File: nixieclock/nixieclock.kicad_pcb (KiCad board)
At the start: 4 copper layers, 91 parts, among them Q1 AO3401A, Q10 BSS131, Q11 BSS131, Q12 BSS131, Q13 BSS131, Q14 BSS131, Q15 BSS131, Q16 BSS131, Q17 BSS131, Q18 BSS131, Q19 BSS131, Q2 IRLR3110ZTRPBF, Q20 BSS131, Q21 BSS131, Q22 BSS131, Q23 BSS131, Q24 BSS131, Q25 BSS131, Q26 BSS131, Q27 BSS131, Q28 BSS131, Q29 BSS131, Q3 BSS131, Q30 BSS131, Q31 BSS131, Q32 BSS131, Q33 BSS131, Q34 BSS131, Q35 BSS131, Q36 BSS131, Q37 BSS131, Q38 BSS131, Q39 BSS131, Q4 BSS131, Q40 BSS131, Q41 BSS131, Q42 BSS131, Q5 BSS131, Q6 BSS131, Q7 BSS131, Q8 BSS131, Q9 BSS131, U1 LT3757AEMSE, U2 AMS1117-3.3, U3 74HC595, U4 74HC595, U5 74HC595, U6 74HC595, U7 74HC595, U8 STM32F058R8Tx

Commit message: mostly finalized pcb layout, silkscreen graphics, etc
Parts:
- added BT1: Battery_Cell, Battery:BatteryHolder_Keystone_3000_1x12mm, F.Cu at (130.0, 99.0)
- added C20: 100nF, Capacitor_SMD:C_0603_1608Metric_Pad1.05x0.95mm_HandSolder, F.Cu at (139.4, 103.4)
- added C21: 100nF, Capacitor_SMD:C_0603_1608Metric_Pad1.05x0.95mm_HandSolder, F.Cu at (154.6, 94.6)
- added C22: 10nF, Capacitor_SMD:C_0603_1608Metric_Pad1.05x0.95mm_HandSolder, F.Cu at (149.0, 106.6)
- added C23: 1uF, Capacitor_SMD:C_0603_1608Metric_Pad1.05x0.95mm_HandSolder, F.Cu at (149.0, 108.2)
- added C24: 100nF, Capacitor_SMD:C_0603_1608Metric_Pad1.05x0.95mm_HandSolder, F.Cu at (146.2, 107.4)
- added G**: ARM-JTAG-10-SILK, Personal:ARM-JTAG-10-SILK, F.Cu at (152.6, 84.8)
- added G***: LOGO, nixieclock_graphics:high_voltage, F.Cu at (117.1, 93.4)
- added G***: LOGO, nixieclock_graphics:db_logo, F.Cu at (122.0, 80.0)
- added J1: USB_C_Receptacle, Connector_USB:USB_C_Receptacle_Amphenol_12401610E4-2A, F.Cu at (80.4, 75.0)
- added J2: Conn_ARM_JTAG_SWD_10, Connector_PinHeader_2.54mm:PinHeader_2x05_P2.54mm_Vertical_SMD, F.Cu at (139.2, 84.8)
- added R14: 10k, Resistor_SMD:R_0603_1608Metric_Pad1.05x0.95mm_HandSolder, F.Cu at (139.4, 100.0)
- U8: value STM32F058R8Tx -> STM32F051R4Tx
- moved C14 62.4 mm to (105.0, 75.3), turned to 180 degrees
- moved F1 61.6 mm to (88.1, 79.9), turned to 0 degrees
- moved Q1 58.4 mm to (93.0, 79.9), turned to 180 degrees
- moved FB1 56.4 mm to (96.5, 80.0), turned to 90 degrees
- moved C13 56.3 mm to (99.0, 80.0), turned to 90 degrees
- moved U2 55.7 mm to (105.0, 80.0), turned to 0 degrees
- moved C5 52.1 mm to (95.0, 83.9), turned to 180 degrees
- moved C18 39.0 mm to (134.4, 159.7), turned to 90 degrees
- moved C16 38.9 mm to (101.0, 159.7), turned to 90 degrees
- moved C17 37.3 mm to (116.0, 152.0), turned to 90 degrees
- moved C15 37.1 mm to (83.5, 162.5), turned to 0 degrees
- moved C19 37.0 mm to (150.0, 162.5), turned to 0 degrees
- moved Q2 36.1 mm to (71.0, 101.1)
- moved C1 36.1 mm to (79.5, 87.0)
- moved C10 36.1 mm to (69.2, 86.4)
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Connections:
- F1 pad 1: (no net) -> +5V
- R3 pad 1: VCC -> +3V3
- R3 pad 2: ~SHDN -> /microcontroller/~SHDN
- U1 pad 9: ~SHDN -> /microcontroller/~SHDN
- U3 pad 14: (no net) -> /cathode_registers/D
- U8 pad 1: unconnected-(U8-Pad1) -> /microcontroller/VBAT
- U8 pad 10: unconnected-(U8-Pad10) -> (no net)
- U8 pad 11: unconnected-(U8-Pad11) -> (no net)
- U8 pad 12: unconnected-(U8-Pad12) -> GND
- U8 pad 13: unconnected-(U8-Pad13) -> +3V3
- U8 pad 14: unconnected-(U8-Pad14) -> /cathode_registers/~OE
- U8 pad 15: unconnected-(U8-Pad15) -> /cathode_registers/~RES
- U8 pad 16: unconnected-(U8-Pad16) -> /cathode_registers/LCLK
- U8 pad 17: unconnected-(U8-Pad17) -> /microcontroller/~SHDN
- U8 pad 18: unconnected-(U8-Pad18) -> (no net)
- U8 pad 19: unconnected-(U8-Pad19) -> (no net)
- U8 pad 2: unconnected-(U8-Pad2) -> (no net)
- U8 pad 20: unconnected-(U8-Pad20) -> (no net)
- U8 pad 21: unconnected-(U8-Pad21) -> /cathode_registers/CLK
- U8 pad 22: unconnected-(U8-Pad22) -> (no net)
- U8 pad 23: unconnected-(U8-Pad23) -> /cathode_registers/D
- U8 pad 24: unconnected-(U8-Pad24) -> (no net)
- U8 pad 25: unconnected-(U8-Pad25) -> (no net)
- U8 pad 26: unconnected-(U8-Pad26) -> (no net)
- U8 pad 27: unconnected-(U8-Pad27) -> (no net)
- U8 pad 28: unconnected-(U8-Pad28) -> (no net)
- U8 pad 29: unconnected-(U8-Pad29) -> (no net)
- U8 pad 3: unconnected-(U8-Pad3) -> (no net)
- U8 pad 30: unconnected-(U8-Pad30) -> (no net)
- U8 pad 31: unconnected-(U8-Pad31) -> GND
- U8 pad 32: unconnected-(U8-Pad32) -> +3V3
- U8 pad 33: unconnected-(U8-Pad33) -> (no net)
- U8 pad 34: unconnected-(U8-Pad34) -> (no net)
- U8 pad 35: unconnected-(U8-Pad35) -> (no net)
- U8 pad 36: unconnected-(U8-Pad36) -> (no net)
- U8 pad 37: unconnected-(U8-Pad37) -> (no net)
- U8 pad 38: unconnected-(U8-Pad38) -> (no net)
- U8 pad 39: unconnected-(U8-Pad39) -> (no net)
- U8 pad 4: unconnected-(U8-Pad4) -> (no net)
- U8 pad 40: unconnected-(U8-Pad40) -> (no net)
- U8 pad 41: unconnected-(U8-Pad41) -> (no net)
- U8 pad 42: unconnected-(U8-Pad42) -> (no net)
- U8 pad 43: unconnected-(U8-Pad43) -> (no net)
- U8 pad 44: unconnected-(U8-Pad44) -> (no net)
- U8 pad 45: unconnected-(U8-Pad45) -> (no net)
- U8 pad 46: unconnected-(U8-Pad46) -> /microcontroller/SWDIO
- U8 pad 47: unconnected-(U8-Pad47) -> (no net)
- U8 pad 48: unconnected-(U8-Pad48) -> (no net)
- U8 pad 49: unconnected-(U8-Pad49) -> /microcontroller/SWDCLK
- U8 pad 5: unconnected-(U8-Pad5) -> (no net)
- U8 pad 50: unconnected-(U8-Pad50) -> (no net)
- U8 pad 51: unconnected-(U8-Pad51) -> (no net)
- U8 pad 52: unconnected-(U8-Pad52) -> (no net)
- U8 pad 53: unconnected-(U8-Pad53) -> (no net)
- U8 pad 54: unconnected-(U8-Pad54) -> (no net)
- U8 pad 55: unconnected-(U8-Pad55) -> (no net)
- U8 pad 56: unconnected-(U8-Pad56) -> (no net)
- U8 pad 57: unconnected-(U8-Pad57) -> (no net)
- U8 pad 58: unconnected-(U8-Pad58) -> (no net)
- U8 pad 59: unconnected-(U8-Pad59) -> (no net)
- U8 pad 6: unconnected-(U8-Pad6) -> (no net)
- U8 pad 60: unconnected-(U8-Pad60) -> Net-(R14-Pad2)
- U8 pad 61: unconnected-(U8-Pad61) -> (no net)
- U8 pad 62: unconnected-(U8-Pad62) -> (no net)
- U8 pad 63: unconnected-(U8-Pad63) -> GND
- U8 pad 64: unconnected-(U8-Pad64) -> +3V3
- U8 pad 7: unconnected-(U8-Pad7) -> /microcontroller/~NRST
- U8 pad 8: unconnected-(U8-Pad8) -> (no net)
- U8 pad 9: unconnected-(U8-Pad9) -> (no net)
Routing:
- net /cathode_registers/~OE: track 0.00 -> 176.0 mm, vias 0 -> 5
- net /cathode_registers/CLK: track 0.00 -> 170.9 mm
- net /cathode_registers/LCLK: track 0.00 -> 158.7 mm, vias 0 -> 5
- net /cathode_registers/~RES: track 0.00 -> 146.0 mm, vias 0 -> 6
- net /cathode_registers/D: track 0.00 -> 144.1 mm, vias 0 -> 2
- net /microcontroller/~SHDN: track 0.00 -> 88.8 mm, vias 0 -> 2
- net GND: track 119.1 -> 166.6 mm, vias 139 -> 173
- net /microcontroller/VBAT: track 0.00 -> 32.6 mm
- net /microcontroller/~NRST: track 0.00 -> 27.4 mm, vias 0 -> 2
- net +3V3: track 12.4 -> 37.2 mm, vias 0 -> 21
- net HV: track 74.6 -> 86.3 mm
- net /microcontroller/SWDCLK: track 0.00 -> 8.08 mm
- net /microcontroller/SWDIO: track 0.00 -> 7.04 mm
- net ~SHDN: track 5.67 -> 0.00 mm
- net Net-(U5-Pad9): track 20.7 -> 17.2 mm, vias 0 -> 2
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- added copper zone on F.Cu, net (none)
- added copper zone on F.Cu, net +3V3
- added copper zone on In2.Cu, net +3V3
- added copper zone on F.Cu, net +5V
- added copper zone on B.Cu, net GND
- added copper zone on F.Cu, net GND
- added copper zone on In1.Cu, net GND
- added copper zone on F.Cu, net Net-(FB1-Pad2)
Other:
- board outline added: 96.5 x 95 mm
- board text added: "+"
- board text added: "DANGER! HIGH VOLTAGE"
- board text removed: "DANGER: HIGH VOLTAGE"

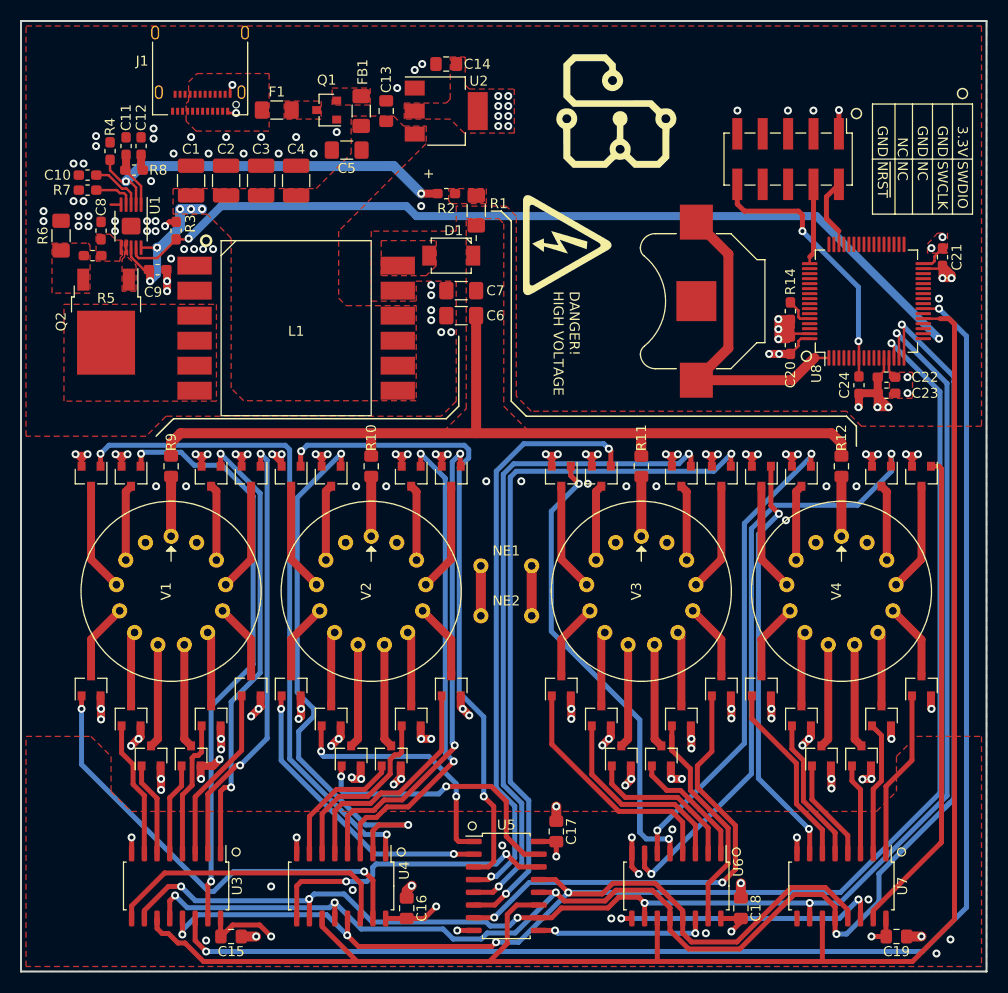
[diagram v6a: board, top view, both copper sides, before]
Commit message: finalized neon bulb design (todo: pcb jumpers)
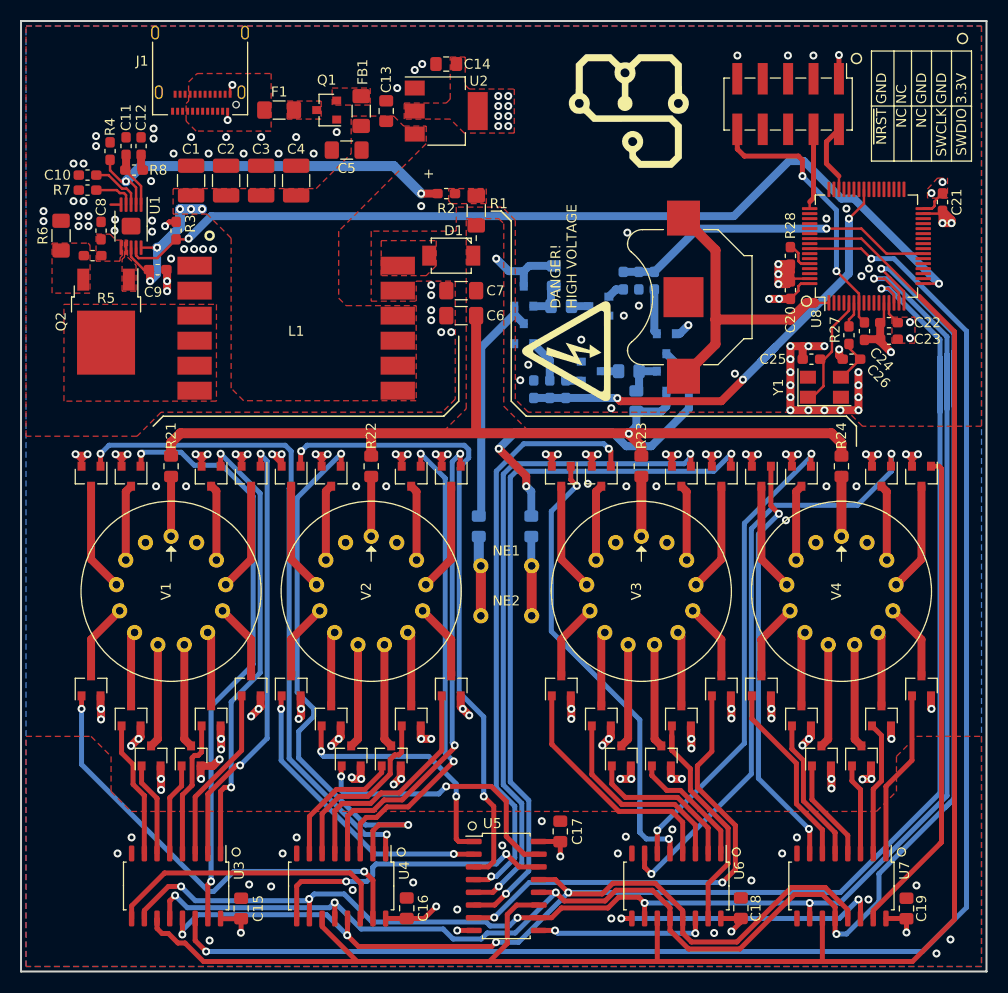
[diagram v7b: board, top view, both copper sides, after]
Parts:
- added C25: 24pF, Capacitor_SMD:C_0603_1608Metric_Pad1.05x0.95mm_HandSolder, F.Cu at (141.5, 104.8)
- added C26: 24pF, Capacitor_SMD:C_0603_1608Metric_Pad1.05x0.95mm_HandSolder, F.Cu at (145.5, 104.8)
- added Q3: BSR92P, Package_TO_SOT_SMD:SOT-23, B.Cu at (112.8, 98.5)
- added Q4: BSR92P, Package_TO_SOT_SMD:SOT-23, B.Cu at (127.0, 107.0)
- added Q5: BSS131, Package_TO_SOT_SMD:SOT-23, B.Cu at (120.2, 99.5)
- added Q6: BSS131, Package_TO_SOT_SMD:SOT-23, B.Cu at (119.5, 106.0)
- added Q7: BSS131, Package_TO_SOT_SMD:SOT-23, B.Cu at (112.8, 102.2)
- added Q8: BSS131, Package_TO_SOT_SMD:SOT-23, B.Cu at (127.0, 103.2)
- added R10: 10k, Resistor_SMD:R_0805_2012Metric_Pad1.15x1.40mm_HandSolder, B.Cu at (124.0, 109.0)
- added R11: 160k, Resistor_SMD:R_0805_2012Metric_Pad1.15x1.40mm_HandSolder, B.Cu at (116.5, 99.5)
- added R12: 160k, Resistor_SMD:R_0805_2012Metric_Pad1.15x1.40mm_HandSolder, B.Cu at (123.2, 106.0)
- added R13: 100, Resistor_SMD:R_0603_1608Metric_Pad1.05x0.95mm_HandSolder, B.Cu at (122.7, 97.0)
- added R15: R_Small, Resistor_SMD:R_0603_1608Metric_Pad1.05x0.95mm_HandSolder, B.Cu at (124.2, 97.0)
- added R16: R_Small, Resistor_SMD:R_0603_1608Metric_Pad1.05x0.95mm_HandSolder, B.Cu at (113.8, 107.8)
- added R17: 100, Resistor_SMD:R_0603_1608Metric_Pad1.05x0.95mm_HandSolder, B.Cu at (115.3, 107.8)
- added R18: 100, Resistor_SMD:R_0603_1608Metric_Pad1.05x0.95mm_HandSolder, B.Cu at (125.8, 97.0)
- added R25: 68k, Resistor_SMD:R_0805_2012Metric_Pad1.15x1.40mm_HandSolder, B.Cu at (108.2, 121.5)
- added R26: 68k, Resistor_SMD:R_0805_2012Metric_Pad1.15x1.40mm_HandSolder, B.Cu at (113.5, 121.5)
- added R27: ?, Resistor_SMD:R_0603_1608Metric_Pad1.05x0.95mm_HandSolder, F.Cu at (145.2, 102.4)
- added R28: 10k, Resistor_SMD:R_0603_1608Metric_Pad1.05x0.95mm_HandSolder, F.Cu at (139.4, 94.5)
- added R9: 10k, Resistor_SMD:R_0805_2012Metric_Pad1.15x1.40mm_HandSolder, B.Cu at (115.8, 96.5)
- added Y1: 8MHz, Crystal:Crystal_SMD_5032-4Pin_5.0x3.2mm, F.Cu at (142.8, 107.6)
- R14: value 10k -> 100; moved to B.Cu
- R21: renamed from R9; footprint Capacitor_SMD:C_0805_2012Metric_Pad1.15x1.40mm_HandSolder -> Resistor_SMD:R_0805_2012Metric_Pad1.15x1.40mm_HandSolder
- R22: renamed from R10; value R -> 10k
- R23: renamed from R11; value R -> 10k
- R24: renamed from R12; value R -> 10k
- moved R14 23.8 mm to (117.0, 107.8)
- moved G*** 10.6 mm to (117.0, 104.0), turned to 90 degrees
- moved C20 5.50 mm to (139.4, 97.9)
- moved C21 5.50 mm to (154.6, 89.1)
- moved J2 5.50 mm to (139.2, 79.3)
- moved U8 5.50 mm to (147.0, 93.5)
- moved C22 5.46 mm to (149.2, 101.2)
- moved C24 5.43 mm to (146.8, 102.0)
- moved C23 5.41 mm to (149.2, 102.8)
- moved G** 5.30 mm to (152.5, 79.5)
- moved C15 2.97 mm to (84.5, 159.7), turned to 90 degrees
- moved C19 2.97 mm to (151.0, 159.7), turned to 90 degrees
- moved BT1 1.35 mm to (128.7, 98.6)
- moved G*** 1.25 mm to (123.2, 80.0), turned to 90 degrees
- moved C17 0.40 mm to (116.4, 152.0)
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- renumbered Q4 to Q10, Q5 to Q11, Q6 to Q12, Q7 to Q13, Q8 to Q14, Q9 to Q15, Q10 to Q16, Q11 to Q17, Q12 to Q18, Q13 to Q19, Q14 to Q20, Q15 to Q21, Q16 to Q22, Q17 to Q23, Q18 to Q24, Q19 to Q25, Q20 to Q26, Q21 to Q27, Q22 to Q28, Q23 to Q29, Q24 to Q30, Q25 to Q31, Q26 to Q32, Q27 to Q33, Q28 to Q34, Q29 to Q35, Q30 to Q36, Q31 to Q37, Q32 to Q38, Q33 to Q39, Q34 to Q40, Q35 to Q41, Q36 to Q42, Q37 to Q43, Q38 to Q44, Q39 to Q45, Q40 to Q46, Q41 to Q47, Q42 to Q48, Q3 to Q9
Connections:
- net /nixie_tubes/NEH+ renamed Net-(NE1-Pad2)
- net /nixie_tubes/NEH- renamed Net-(NE1-Pad1)
- J2 pad 6: unconnected-(J2-Pad6) -> (no net)
- J2 pad 7: unconnected-(J2-Pad7) -> (no net)
- J2 pad 8: unconnected-(J2-Pad8) -> (no net)
- R14 pad 1: GND -> /microcontroller/TIM1_CH1
- R14 pad 2: Net-(R14-Pad2) -> Net-(Q6-Pad1)
- U8 pad 21: /cathode_registers/CLK -> (no net)
- U8 pad 23: /cathode_registers/D -> /microcontroller/~TIM1_CH1N
- U8 pad 41: (no net) -> /microcontroller/TIM1_CH1
- U8 pad 5: (no net) -> /microcontroller/OSC_IN
- U8 pad 55: (no net) -> /cathode_registers/CLK
- U8 pad 57: (no net) -> /cathode_registers/D
- U8 pad 6: (no net) -> /microcontroller/OSC_OUT
- U8 pad 60: Net-(R14-Pad2) -> Net-(R28-Pad2)
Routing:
- net /microcontroller/TIM1_CH1: track 0.00 -> 47.9 mm, vias 0 -> 3
- net /nixie_tubes/NEH-: track 0.00 -> 36.3 mm, vias 0 -> 2
- net /microcontroller/~TIM1_CH1N: track 0.00 -> 32.8 mm, vias 0 -> 1
- net /nixie_tubes/NEH+: track 0.00 -> 23.8 mm
- net /cathode_registers/D: track 144.1 -> 163.8 mm
- net /cathode_registers/CLK: track 170.9 -> 190.1 mm
- net HV: track 86.3 -> 102.1 mm, vias 0 -> 2
- net /cathode_registers/~RES: track 146.0 -> 160.3 mm
- net /cathode_registers/LCLK: track 158.7 -> 172.0 mm
- net /cathode_registers/~OE: track 176.0 -> 188.6 mm
- net /microcontroller/OSC_IN: track 0.00 -> 11.9 mm
- net Net-(C26-Pad1): track 0.00 -> 5.51 mm
- net Net-(Q8-Pad1): track 0.00 -> 4.53 mm
- net Net-(Q7-Pad1): track 0.00 -> 4.36 mm
- net GND: track 166.6 -> 170.9 mm, vias 173 -> 199
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- added copper zone on F.Cu, net Net-(F1-Pad2)
- removed copper zone on F.Cu, net (none)

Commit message: finalized layout, added encoder
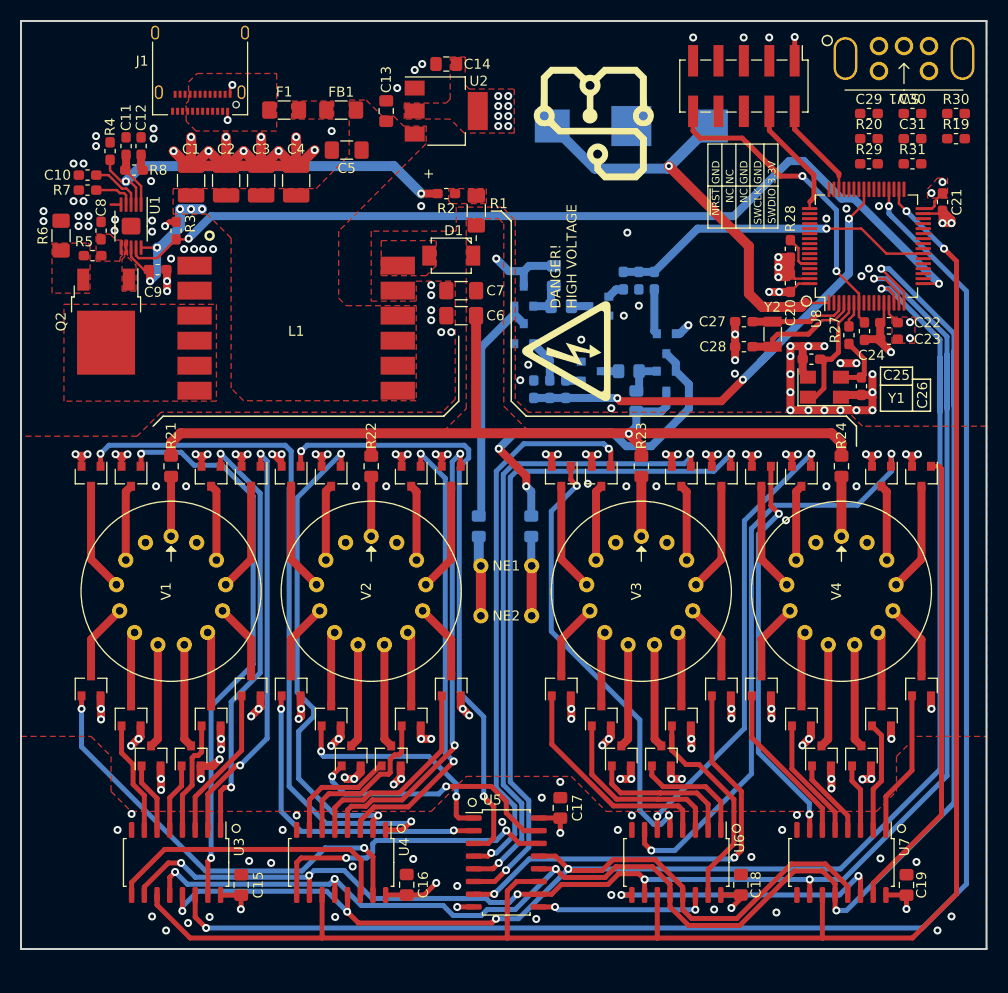
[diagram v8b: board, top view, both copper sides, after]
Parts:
- removed Q1: AO3401A, Package_TO_SOT_SMD:SOT-23
- added C27: 15pF, Capacitor_SMD:C_0603_1608Metric_Pad1.05x0.95mm_HandSolder, F.Cu at (134.8, 101.0)
- added C28: 15pF, Capacitor_SMD:C_0603_1608Metric_Pad1.05x0.95mm_HandSolder, F.Cu at (134.8, 103.5)
- added C29: 10nF, Capacitor_SMD:C_0603_1608Metric_Pad1.05x0.95mm_HandSolder, F.Cu at (147.2, 80.2)
- added C30: 10nF, Capacitor_SMD:C_0603_1608Metric_Pad1.05x0.95mm_HandSolder, F.Cu at (151.6, 80.2)
- added C31: 10nF, Capacitor_SMD:C_0603_1608Metric_Pad1.05x0.95mm_HandSolder, F.Cu at (151.6, 82.8)
- added R19: 10k, Resistor_SMD:R_0603_1608Metric_Pad1.05x0.95mm_HandSolder, F.Cu at (155.9, 82.8)
- added R20: 10k, Resistor_SMD:R_0603_1608Metric_Pad1.05x0.95mm_HandSolder, F.Cu at (147.2, 82.8)
- added R29: 10k, Resistor_SMD:R_0603_1608Metric_Pad1.05x0.95mm_HandSolder, F.Cu at (147.2, 85.3)
- added R30: 10k, Resistor_SMD:R_0603_1608Metric_Pad1.05x0.95mm_HandSolder, F.Cu at (155.9, 80.2)
- added R31: 10k, Resistor_SMD:R_0603_1608Metric_Pad1.05x0.95mm_HandSolder, F.Cu at (151.6, 85.3)
- added SW1: EN11-VSM, Personal:EN11-VSM1AF20, F.Cu at (150.8, 74.8)
- added Y2: 32.768kHz, Crystal:Crystal_SMD_3215-2Pin_3.2x1.5mm, F.Cu at (137.6, 102.3)
- BT1: moved to B.Cu
- C25, C26: value 24pF -> 10pF
- R27: value ? -> 22
- moved G** 19.5 mm to (134.8, 87.5)
- moved BT1 17.9 mm to (123.5, 81.5), turned to 0 degrees
- moved J2 4.77 mm to (134.8, 77.5)
- moved G2 3.72 mm to (119.8, 81.2)
- moved C26 2.88 mm to (146.5, 107.5), turned to -90 degrees
- moved C16 2.35 mm to (101.0, 157.3)
- moved C18 2.35 mm to (134.4, 157.3)
- moved C15 2.35 mm to (84.5, 157.3)
- moved C17 2.35 mm to (116.4, 149.7)
- moved C19 2.35 mm to (151.0, 157.3)
- moved U3 2.35 mm to (78.0, 155.1)
- moved U4 2.35 mm to (94.5, 155.1)
- moved U5 2.35 mm to (111.0, 155.1)
- moved U6 2.35 mm to (128.0, 155.1)
- moved U7 2.35 mm to (144.5, 155.1)
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- renumbered G*** to G1, G*** to G2
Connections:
- FB1 pad 2: Net-(FB1-Pad2) -> Net-(F1-Pad2)
- U8 pad 3: (no net) -> /microcontroller/OSC32_IN
- U8 pad 34: (no net) -> /cathode_registers/CLK
- U8 pad 36: (no net) -> /cathode_registers/D
- U8 pad 4: (no net) -> /microcontroller/OSC32_OUT
- U8 pad 55: /cathode_registers/CLK -> (no net)
- U8 pad 57: /cathode_registers/D -> (no net)
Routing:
- net GND: track 170.9 -> 222.3 mm, vias 199 -> 208
- net /microcontroller/VBAT: track 30.5 -> 50.0 mm, vias 0 -> 1
- net /microcontroller/OSC32_OUT: track 0.00 -> 11.9 mm
- net /cathode_registers/CLK: track 190.1 -> 178.4 mm, vias 0 -> 2
- net /microcontroller/OSC32_IN: track 0.00 -> 9.86 mm
- net /cathode_registers/GB8: track 29.6 -> 39.2 mm
- net /microcontroller/~NRST: track 27.7 -> 36.8 mm
- net /cathode_registers/LCLK: track 172.0 -> 179.5 mm
- net /cathode_registers/GB0: track 54.6 -> 48.0 mm
- net /cathode_registers/GA9: track 66.5 -> 71.4 mm
- net /cathode_registers/GC9: track 49.2 -> 44.8 mm
- net /cathode_registers/D: track 163.8 -> 159.7 mm
- net /microcontroller/SWDCLK: track 8.08 -> 11.7 mm
- net /cathode_registers/GB1: track 48.3 -> 45.4 mm
- net /microcontroller/SWDIO: track 7.04 -> 9.63 mm
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- added copper zone on F.Cu, net (none)
- removed copper zone on F.Cu, net Net-(F1-Pad2)
- removed copper zone on F.Cu, net Net-(FB1-Pad2)
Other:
- board size 96.5 x 95 mm -> 96.5 x 92.8 mm
- board text added: "HV"
